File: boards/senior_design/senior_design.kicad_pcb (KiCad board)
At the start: 2 copper layers, 55 parts, among them IC1 MAX038*, IC2 MAX038*, J1 Conn_2Rows-09Pins, U1 AD620, U10 ATmega328-P, U11 UA741CP, U12 UA741CP, U13 UA741CP, U2 AD620, U3 AD620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

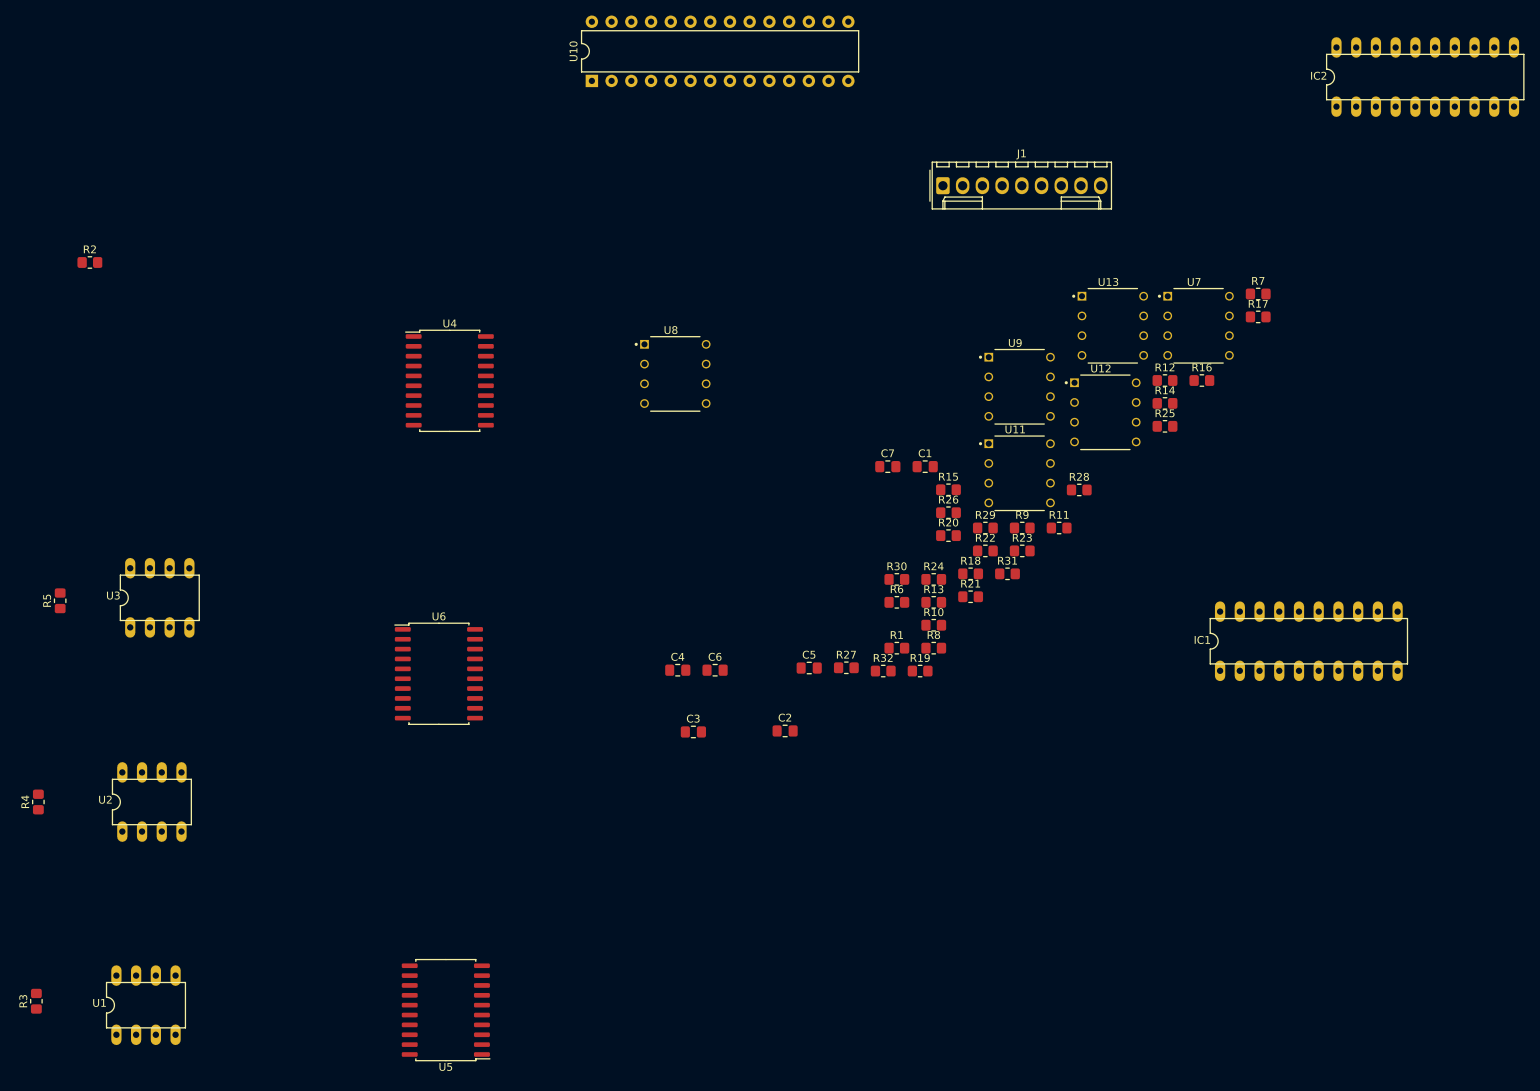
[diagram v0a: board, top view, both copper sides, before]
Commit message: changed schematic for 4 boards instead of 1
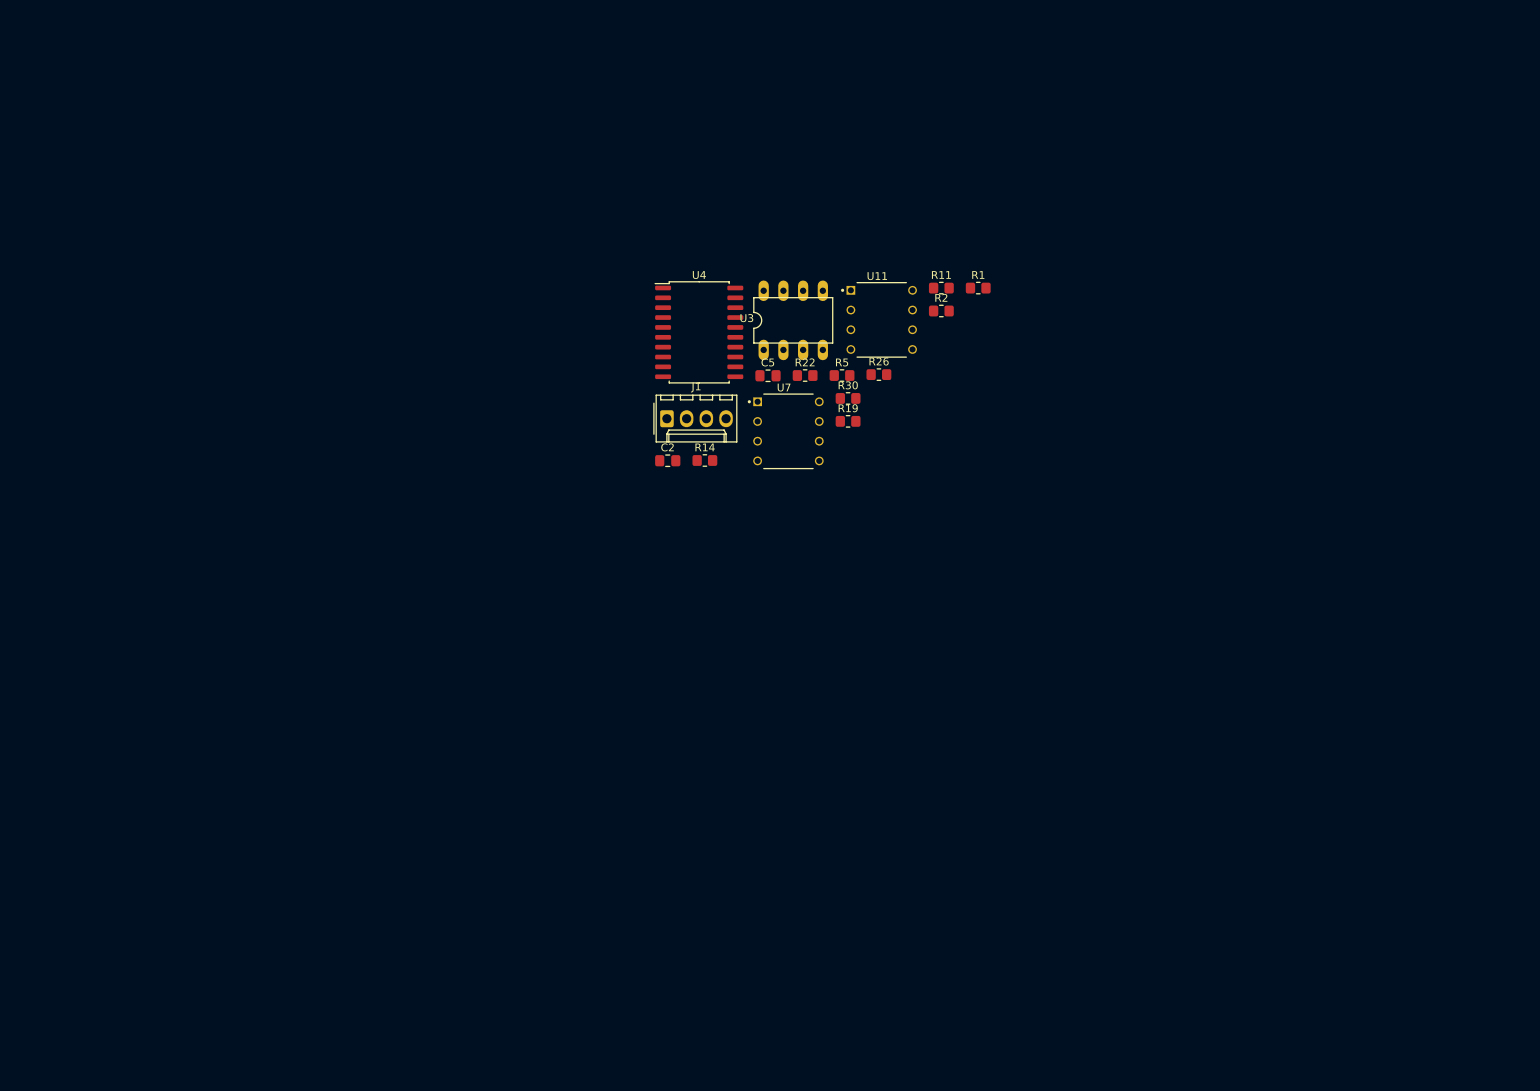
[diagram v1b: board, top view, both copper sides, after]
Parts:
- removed C1, C3, C4: 1uF, Capacitor_SMD:C_0805_2012Metric_Pad1.18x1.45mm_HandSolder
- removed C6, C7: 200nF, Capacitor_SMD:C_0805_2012Metric_Pad1.18x1.45mm_HandSolder
- removed IC1, IC2: MAX038*, MAX038:DIL20
- removed R10, R12, R13, R15, R16, R17, R18, R23, R24, R25, R27, R28, R29, R3, R31, R32, R4: 1K, Resistor_SMD:R_0805_2012Metric_Pad1.20x1.40mm_HandSolder
- removed R20, R21: 200K, Resistor_SMD:R_0805_2012Metric_Pad1.20x1.40mm_HandSolder
- removed R6, R7, R8, R9: 10K, Resistor_SMD:R_0805_2012Metric_Pad1.20x1.40mm_HandSolder
- removed U1, U2: AD620, AD620:DIL08
- removed U10: ATmega328-P, Package_DIP:DIP-28_W7.62mm
- removed U12, U13, U8, U9: UA741CP, uA741:DIP794W45P254L959H508Q8
- removed U5, U6: AD630ARZ, Package_SO:SOIC-20W_7.5x12.8mm_P1.27mm
- J1: value Conn_2Rows-09Pins -> Conn_01x04; footprint Connector_Molex:Molex_KK-254_AE-6410-09A_1x09_P2.54mm_Vertical -> Connector_Molex:Molex_KK-254_AE-6410-04A_1x04_P2.54mm_Vertical
- moved R2 109.8 mm to (146.5, 62.0)
- moved R5 104.8 mm to (133.7, 70.3), turned to 0 degrees
- moved U3 89.0 mm to (127.4, 63.2)
- moved R14 59.7 mm to (116.0, 81.2)
- moved U7 54.5 mm to (126.8, 77.5)
- moved R1 47.5 mm to (151.2, 59.0)
- moved J1 46.5 mm to (111.1, 75.9)
- moved C5 38.0 mm to (124.2, 70.3)
- moved C2 37.9 mm to (111.3, 81.3)
- moved R11 34.4 mm to (146.5, 59.0)
- moved R19 33.5 mm to (134.5, 76.2)
- moved U4 32.7 mm to (115.3, 64.8)
- moved R22 32.4 mm to (128.9, 70.3)
- moved U11 26.6 mm to (138.8, 63.1)
- moved R30 24.1 mm to (134.5, 73.3)
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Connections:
- J1 pad 1: Net-(J1-Pad1) -> Net-(U4-Pad10)
- J1 pad 2: Net-(IC1-Pad19) -> GND
- J1 pad 3: Net-(IC1-Pad19) -> Net-(R1-Pad1)
- J1 pad 4: Net-(J1-Pad4) -> Net-(R2-Pad1)
- R1 pad 1: Net-(J1-Pad1) -> Net-(R1-Pad1)
- R2 pad 1: Net-(J1-Pad5) -> Net-(R2-Pad1)
- U3 pad 2: Net-(J1-Pad8) -> Net-(R2-Pad1)
- U3 pad 3: Net-(J1-Pad4) -> Net-(R1-Pad1)
- U4 pad 10: Net-(C1-Pad2) -> Net-(U4-Pad10)
